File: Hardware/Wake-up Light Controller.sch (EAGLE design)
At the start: 47 parts, among them IC1 ST1S10, IC2 HT7333, IC3 DS3231/SO, IC4 ATMEGA328P_TQFP, J1 AVR-ISP, J2 Debug, Q1 BSS138, Q2 BSS138, Q3 FDN306P, Q4 IRLZ44N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

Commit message: Changed battery holder name
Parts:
- renumbered U$1 to J3
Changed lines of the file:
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@@
 <grid distance="0.1" unitdist="inch" unit="inch" style="lines" multiple="1" display="no" altdistance="0.01" altunitdist="inch" altunit="inch"/>
 <layers>
-<layer number="1" name="Top" color="4" fill="1" visible="no" active="no"/>
-<layer number="2" name="Route2" color="1" fill="3" visible="no" active="no"/>
-<layer number="3" name="Route3" color="4" fill="3" visible="no" active="no"/>
-<layer number="4" name="Route4" color="1" fill="4" visible="no" active="no"/>
-<layer number="5" name="Route5" color="4" fill="4" visible="no" active="no"/>
-<layer number="6" name="Route6" color="1" fill="8" visible="no" active="no"/>
-<layer number="7" name="Route7" color="4" fill="8" visible="no" active="no"/>
-<layer number="8" name="Route8" color="1" fill="2" visible="no" active="no"/>
-<layer number="9" name="Route9" color="4" fill="2" visible="no" active="no"/>
-<layer number="10" name="Route10" color="1" fill="7" visible="no" active="no"/>
-<layer number="11" name="Route11" color="4" fill="7" visible="no" active="no"/>
-<layer number="12" name="Route12" color="1" fill="5" visible="no" active="no"/>
-<layer number="13" name="Route13" color="4" fill="5" visible="no" active="no"/>
-<layer number="14" name="Route14" color="1" fill="6" visible="no" active="no"/>
-<layer number="15" name="Route15" color="4" fill="6" visible="no" active="no"/>
-<layer number="16" name="Bottom" color="1" fill="1" visible="no" active="no"/>
-<layer number="17" name="Pads" color="2" fill="1" visible="no" active="no"/>
-<layer number="18" name="Vias" color="2" fill="1" visible="no" active="no"/>
-<layer number="19" name="Unrouted" color="6" fill="1" visible="no" active="no"/>
-<layer number="20" name="Dimension" color="24" fill="1" visible="no" active="no"/>
-<layer number="21" name="tPlace" color="7" fill="1" visible="no" active="no"/>
-<layer number="22" name="bPlace" color="7" fill="1" visible="no" active="no"/>
-<layer number="23" name="tOrigins" color="15" fill="1" visible="no" active="no"/>
-<layer number="24" name="bOrigins" color="15" fill="1" visible="no" active="no"/>
-<layer number="25" name="tNames" color="7" fill="1" visible="no" active="no"/>
-<layer number="26" name="bNames" color="7" fill="1" visible="no" active="no"/>
-<layer number="27" name="tValues" color="7" fill="1" visible="no" active="no"/>
-<layer number="28" name="bValues" color="7" fill="1" visible="no" active="no"/>
+<layer number="1" name="Top" color="4" fill="1" visible="yes" active="no"/>
+<layer number="2" name="Route2" color="1" fill="3" visible="yes" active="no"/>
+<layer number="3" name="Route3" color="4" fill="3" visible="yes" active="no"/>
+<layer number="4" name="Route4" color="1" fill="4" visible="yes" active="no"/>
+<layer number="5" name="Route5" color="4" fill="4" visible="yes" active="no"/>
+<layer number="6" name="Route6" color="1" fill="8" visible="yes" active="no"/>
+<layer number="7" name="Route7" color="4" fill="8" visible="yes" active="no"/>
+<layer number="8" name="Route8" color="1" fill="2" visible="yes" active="no"/>
+<layer number="9" name="Route9" color="4" fill="2" visible="yes" active="no"/>
+<layer number="10" name="Route10" color="1" fill="7" visible="yes" active="no"/>
+<layer number="11" name="Route11" color="4" fill="7" visible="yes" active="no"/>
+<layer number="12" name="Route12" color="1" fill="5" visible="yes" active="no"/>
+<layer number="13" name="Route13" color="4" fill="5" visible="yes" active="no"/>
+<layer number="14" name="Route14" color="1" fill="6" visible="yes" active="no"/>
+<layer number="15" name="Route15" color="4" fill="6" visible="yes" active="no"/>
+<layer number="16" name="Bottom" color="1" fill="1" visible="yes" active="no"/>
+<layer number="17" name="Pads" color="2" fill="1" visible="yes" active="no"/>
+<layer number="18" name="Vias" color="2" fill="1" visible="yes" active="no"/>
+<layer number="19" name="Unrouted" color="6" fill="1" visible="yes" active="no"/>
+<layer number="20" name="Dimension" color="24" fill="1" visible="yes" active="no"/>
+<layer number="21" name="tPlace" color="7" fill="1" visible="yes" active="no"/>
+<layer number="22" name="bPlace" color="7" fill="1" visible="yes" active="no"/>
+<layer number="23" name="tOrigins" color="15" fill="1" visible="yes" active="no"/>
+<layer number="24" name="bOrigins" color="15" fill="1" visible="yes" active="no"/>
+<layer number="25" name="tNames" color="7" fill="1" visible="yes" active="no"/>
+<layer number="26" name="bNames" color="7" fill="1" visible="yes" active="no"/>
+<layer number="27" name="tValues" color="7" fill="1" visible="yes" active="no"/>
+<layer number="28" name="bValues" color="7" fill="1" visible="yes" active="no"/>
 <layer number="29" name="tStop" color="7" fill="3" visible="no" active="no"/>
 <layer number="30" name="bStop" color="7" fill="6" visible="no" active="no"/>
@@
 <layer number="35" name="tGlue" color="7" fill="4" visible="no" active="no"/>
 <layer number="36" name="bGlue" color="7" fill="5" visible="no" active="no"/>
-<layer number="37" name="tTest" color="7" fill="1" visible="no" active="no"/>
-<layer number="38" name="bTest" color="7" fill="1" visible="no" active="no"/>
+<layer number="37" name="tTest" color="7" fill="1" visible="yes" active="no"/>
+<layer number="38" name="bTest" color="7" fill="1" visible="yes" active="no"/>
 <layer number="39" name="tKeepout" color="4" fill="11" visible="no" active="no"/>
 <layer number="40" name="bKeepout" color="1" fill="11" visible="no" active="no"/>
@@
 <layer number="44" name="Drills" color="7" fill="1" visible="no" active="no"/>
 <layer number="45" name="Holes" color="7" fill="1" visible="no" active="no"/>
-<layer number="46" name="Milling" color="3" fill="1" visible="no" active="no"/>
-<layer number="47" name="Measures" color="7" fill="1" visible="no" active="no"/>
-<layer number="48" name="Document" color="7" fill="1" visible="no" active="no"/>
-<layer number="49" name="Reference" color="7" fill="1" visible="no" active="no"/>
-<layer number="50" name="dxf" color="7" fill="1" visible="no" active="no"/>
-<layer number="51" name="tDocu" color="7" fill="1" visible="no" active="no"/>
-<layer number="52" name="bDocu" color="7" fill="1" visible="no" active="no"/>
-<layer number="53" name="tGND_GNDA" color="7" fill="9" visible="no" active="no"/>
-<layer number="54" name="bGND_GNDA" color="1" fill="9" visible="no" active="no"/>
-<layer number="56" name="wert" color="7" fill="1" visible="no" active="no"/>
-<layer number="57" name="tCAD" color="7" fill="1" visible="no" active="no"/>
-<layer number="58" name="bCAD" color="11" fill="1" visible="no" active="no"/>
-<layer number="59" name="tCarbon" color="7" fill="1" visible="no" active="no"/>
-<layer number="60" name="bCarbon" color="7" fill="1" visible="no" active="no"/>
+<layer number="46" name="Milling" color="3" fill="1" visible="yes" active="no"/>
+<layer number="47" name="Measures" color="7" fill="1" visible="yes" active="no"/>
+<layer number="48" name="Document" color="7" fill="1" visible="yes" active="no"/>
+<layer number="49" name="Reference" color="7" fill="1" visible="yes" active="no"/>
+<layer number="50" name="dxf" color="7" fill="1" visible="yes" active="no"/>
+<layer number="51" name="tDocu" color="7" fill="1" visible="yes" active="no"/>
+<layer number="52" name="bDocu" color="7" fill="1" visible="yes" active="no"/>
+<layer number="53" name="tGND_GNDA" color="7" fill="9" visible="yes" active="no"/>
+<layer number="54" name="bGND_GNDA" color="1" fill="9" visible="yes" active="no"/>
+<layer number="56" name="wert" color="7" fill="1" visible="yes" active="no"/>
+<layer number="57" name="tCAD" color="7" fill="1" visible="yes" active="no"/>
+<layer number="58" name="bCAD" color="11" fill="1" visible="yes" active="no"/>
+<layer number="59" name="tCarbon" color="7" fill="1" visible="yes" active="no"/>
+<layer number="60" name="bCarbon" color="7" fill="1" visible="yes" active="no"/>
 <layer number="90" name="Modules" color="5" fill="1" visible="yes" active="yes"/>
 <layer number="91" name="Nets" color="2" fill="1" visible="yes" active="yes"/>
@@
 <part name="R9" library="resistor" library_urn="urn:adsk.eagle:library:348" deviceset="R-EU_" device="M0805" package3d_urn="urn:adsk.eagle:package:26079/1" value="10k"/>
 <part name="P+10" library="supply1" library_urn="urn:adsk.eagle:library:371" deviceset="+5V" device=""/>
-<part name="U$1" library="heol" deviceset="BATTCON_16MM_PTH" device="" value="CR1632_3V"/>
+<part name="J3" library="heol" deviceset="BATTCON_16MM_PTH" device="" value="CR1632_3V"/>
 <part name="P+11" library="supply1" library_urn="urn:adsk.eagle:library:371" deviceset="+5V" device=""/>
 <part name="R10" library="resistor" library_urn="urn:adsk.eagle:library:348" deviceset="R-EU_" device="M0805" package3d_urn="urn:adsk.eagle:package:26079/1" value="330"/>
@@
 <instance part="R9" gate="G$1" x="139.7" y="119.38" rot="R270"/>
 <instance part="P+10" gate="1" x="213.36" y="170.18" rot="R270"/>
-<instance part="U$1" gate="G$1" x="200.66" y="157.48" rot="R270"/>
+<instance part="J3" gate="G$1" x="200.66" y="157.48" rot="R270"/>
 <instance part="P+11" gate="1" x="144.78" y="177.8"/>
 <instance part="R10" gate="G$1" x="66.04" y="88.9" rot="R180"/>
@@
 <wire x1="190.5" y1="147.32" x2="190.5" y2="154.94" width="0.1524" layer="91"/>
 <junction x="182.88" y="147.32"/>
-<pinref part="U$1" gate="G$1" pin="GND"/>
+<pinref part="J3" gate="G$1" pin="GND"/>
 <wire x1="190.5" y1="147.32" x2="200.66" y2="147.32" width="0.1524" layer="91"/>
 <wire x1="200.66" y1="147.32" x2="200.66" y2="149.86" width="0.1524" layer="91"/>
@@
 <wire x1="190.5" y1="165.1" x2="190.5" y2="162.56" width="0.1524" layer="91"/>
 <junction x="190.5" y="165.1"/>
-<pinref part="U$1" gate="G$1" pin="VCC"/>
-</segment>
-</net>
+<pinref part="J3" gate="G$1" pin="VCC"/>
+</segment>
+</net>

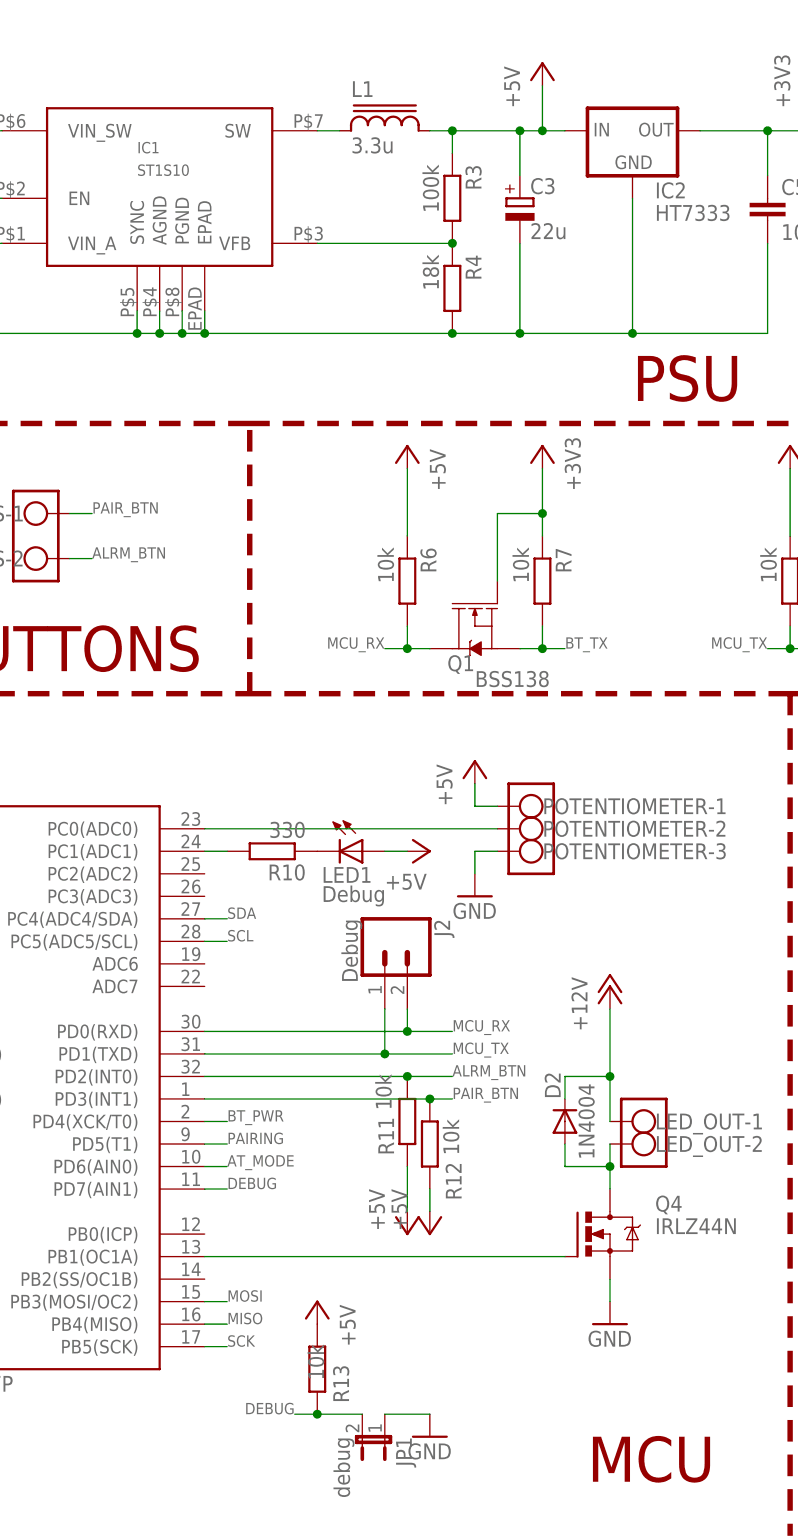
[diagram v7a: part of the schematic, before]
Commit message: Changed inductor package
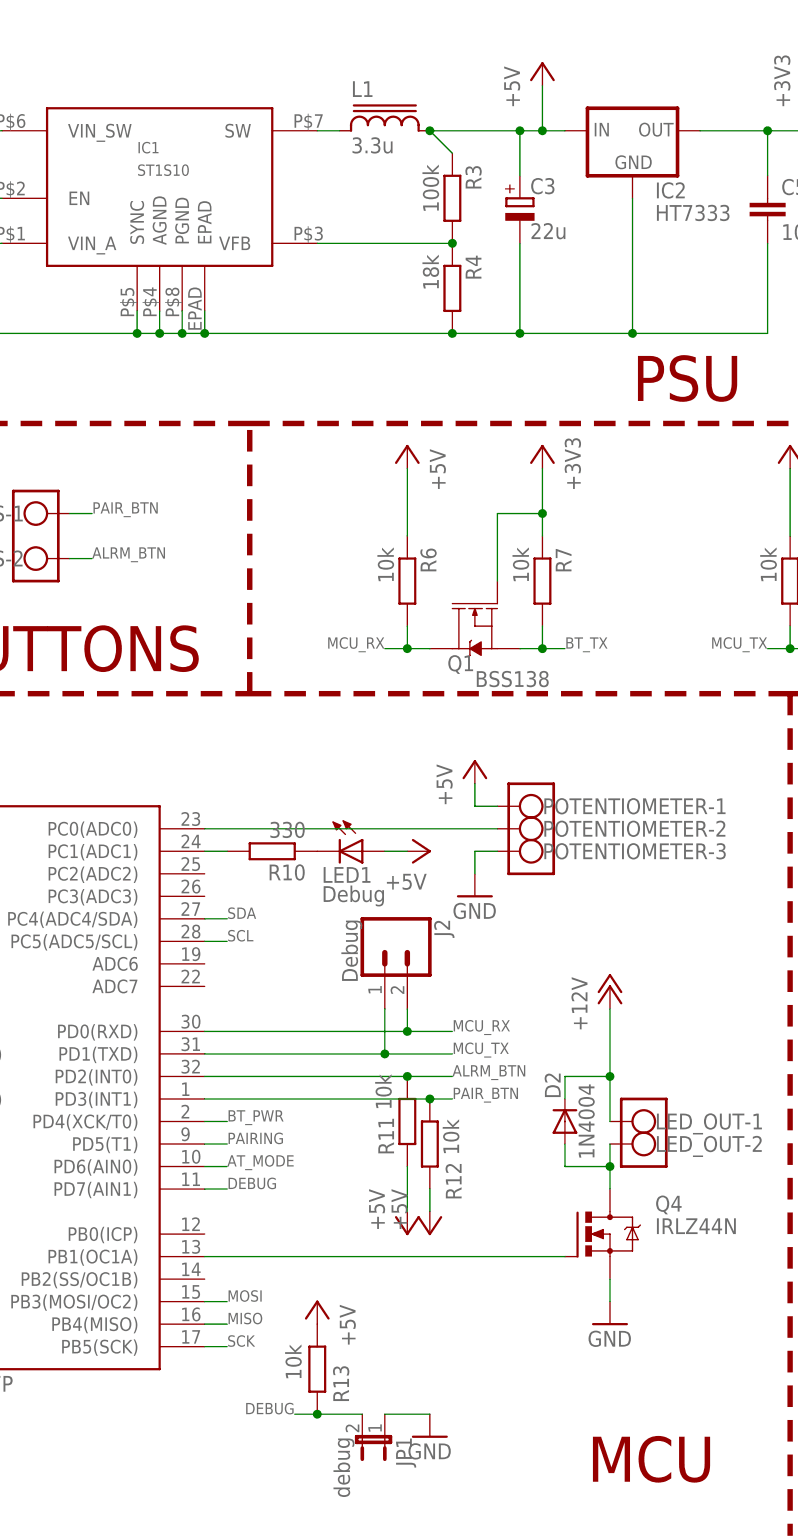
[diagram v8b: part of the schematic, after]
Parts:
- L1: device inductor-sumida:CDRH127/LD -> inductor-wurth:74437346068
- LOGO1: value OSHW-LOGOM-COPPER -> OSHW-LOGOL-COPPER; device SparkFun-Aesthetics:OSHW-LOGOM-COPPER -> SparkFun-Aesthetics:OSHW-LOGOL-COPPER
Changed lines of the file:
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@@
 <part name="R4" library="resistor" library_urn="urn:adsk.eagle:library:348" deviceset="R-EU_" device="M0805" package3d_urn="urn:adsk.eagle:package:26079/1" value="18k"/>
 <part name="R3" library="resistor" library_urn="urn:adsk.eagle:library:348" deviceset="R-EU_" device="M0805" package3d_urn="urn:adsk.eagle:package:26079/1" value="100k"/>
-<part name="L1" library="inductor-sumida" deviceset="CDRH127/LD" device="" value="3.3u"/>
+<part name="L1" library="inductor-wurth" deviceset="74437346068" device="" value="3.3u"/>
 <part name="P+2" library="supply1" library_urn="urn:adsk.eagle:library:371" deviceset="+5V" device=""/>
 <part name="C1" library="rcl" deviceset="C-EU" device="C0805" value="4.7u"/>
@@
 <part name="P+7" library="supply1" library_urn="urn:adsk.eagle:library:371" deviceset="+5V" device=""/>
 <part name="FRAME1" library="frames" library_urn="urn:adsk.eagle:library:229" deviceset="A4L-LOC" device=""/>
-<part name="LOGO1" library="SparkFun-Aesthetics" library_urn="urn:adsk.eagle:library:507" deviceset="OSHW-LOGO" device="M-COPPER" package3d_urn="urn:adsk.eagle:package:37119/1"/>
+<part name="LOGO1" library="SparkFun-Aesthetics" library_urn="urn:adsk.eagle:library:507" deviceset="OSHW-LOGO" device="L-COPPER" package3d_urn="urn:adsk.eagle:package:37117/1" value="OSHW-LOGOL-COPPER"/>
 <part name="GND7" library="supply1" deviceset="GND" device=""/>
 <part name="+3V35" library="supply1" library_urn="urn:adsk.eagle:library:371" deviceset="+3V3" device=""/>
@@
 <instance part="R13" gate="G$1" x="71.12" y="30.48" smashed="yes" rot="R90">
 <attribute name="NAME" x="74.7014" y="26.67" size="1.778" layer="95" rot="R90"/>
-<attribute name="VALUE" x="71.882" y="29.21" size="1.778" layer="96" rot="R90"/>
+<attribute name="VALUE" x="69.342" y="29.21" size="1.778" layer="96" rot="R90"/>
 </instance>
 <instance part="P+15" gate="1" x="71.12" y="38.1" rot="MR0"/>
@@
 <wire x1="93.98" y1="170.18" x2="96.52" y2="170.18" width="0.1524" layer="91"/>
 <pinref part="L1" gate="G$1" pin="2"/>
-<wire x1="83.82" y1="170.18" x2="86.36" y2="170.18" width="0.1524" layer="91"/>
 <junction x="93.98" y="170.18"/>
 <pinref part="R3" gate="G$1" pin="1"/>
-<wire x1="86.36" y1="170.18" x2="93.98" y2="170.18" width="0.1524" layer="91"/>
-<wire x1="86.36" y1="167.64" x2="86.36" y2="170.18" width="0.1524" layer="91"/>
-<junction x="86.36" y="170.18"/>
+<wire x1="83.82" y1="170.18" x2="93.98" y2="170.18" width="0.1524" layer="91"/>
+<wire x1="86.36" y1="167.64" x2="83.82" y2="170.18" width="0.1524" layer="91"/>
+<junction x="83.82" y="170.18"/>
 </segment>
 <segment>
@@
 <segment>
 <pinref part="L1" gate="G$1" pin="1"/>
-<wire x1="73.66" y1="170.18" x2="71.12" y2="170.18" width="0.1524" layer="91"/>
 <pinref part="IC1" gate="G$1" pin="SW"/>
-</segment>
-</net>
+<wire x1="71.12" y1="170.18" x2="73.66" y2="170.18" width="0.1524" layer="91"/>
+</segment>
+</net>
